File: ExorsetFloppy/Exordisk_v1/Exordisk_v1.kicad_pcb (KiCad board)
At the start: 2 copper layers, 160 x 100 mm, 105 parts, among them J1 BUS, J10 Conn_01x01, J11 Conn_01x01, J12 Conn_01x01, J13 Conn_01x01, J14 Conn_01x01, J15 Conn_01x01, J16 Conn_01x01, J17 Conn_01x01, J18 Conn_01x01, J19 Conn_02x02_Odd_Even, J2 Floppy, J20 Conn_01x01, J21 Conn_01x01, J22 Conn_01x01, J23 Conn_01x01, J24 Conn_01x01, J25 Conn_01x01, J26 Conn_01x01, J27 Conn_01x01, J28 Conn_01x01, J29 Conn_01x01, J3 Conn_01x01, J30 Conn_01x01, J31 Conn_01x01, J32 Conn_01x01, J33 Conn_01x01, J34 Conn_01x01, J35 Conn_01x01, J36 Conn_01x01, J37 Conn_01x01, J38 Conn_01x01, J39 Conn_01x01, J4 Conn_01x01, J40 Conn_01x01, J41 Conn_01x01, J5 Conn_01x01, J6 Conn_01x01, J7 Conn_01x17, J8 Conn_01x01, J9 Conn_01x01, Q1 BC337, U1 GAL22V10, U10 GAL16V8, U11 74HCT74, U12 74HCT74, U15 74HCT04, U16 74HCT74, U17 74HCT00, U18 74HCT74, U19 74LS73, U2 74HCT74, U20 68B21, U21 MC4024, U22 74LS157, U23 74LS123, U24 74HCT164, U25 74LS04, U27 MC4044, U28 74F163, U29 74F163, U3 74HC245, U34 6852_DIL24, U4 MC8506_new, U5 74F163, U6 27C32, U7 74HCT240, U8 74HCT244, Y1 1M

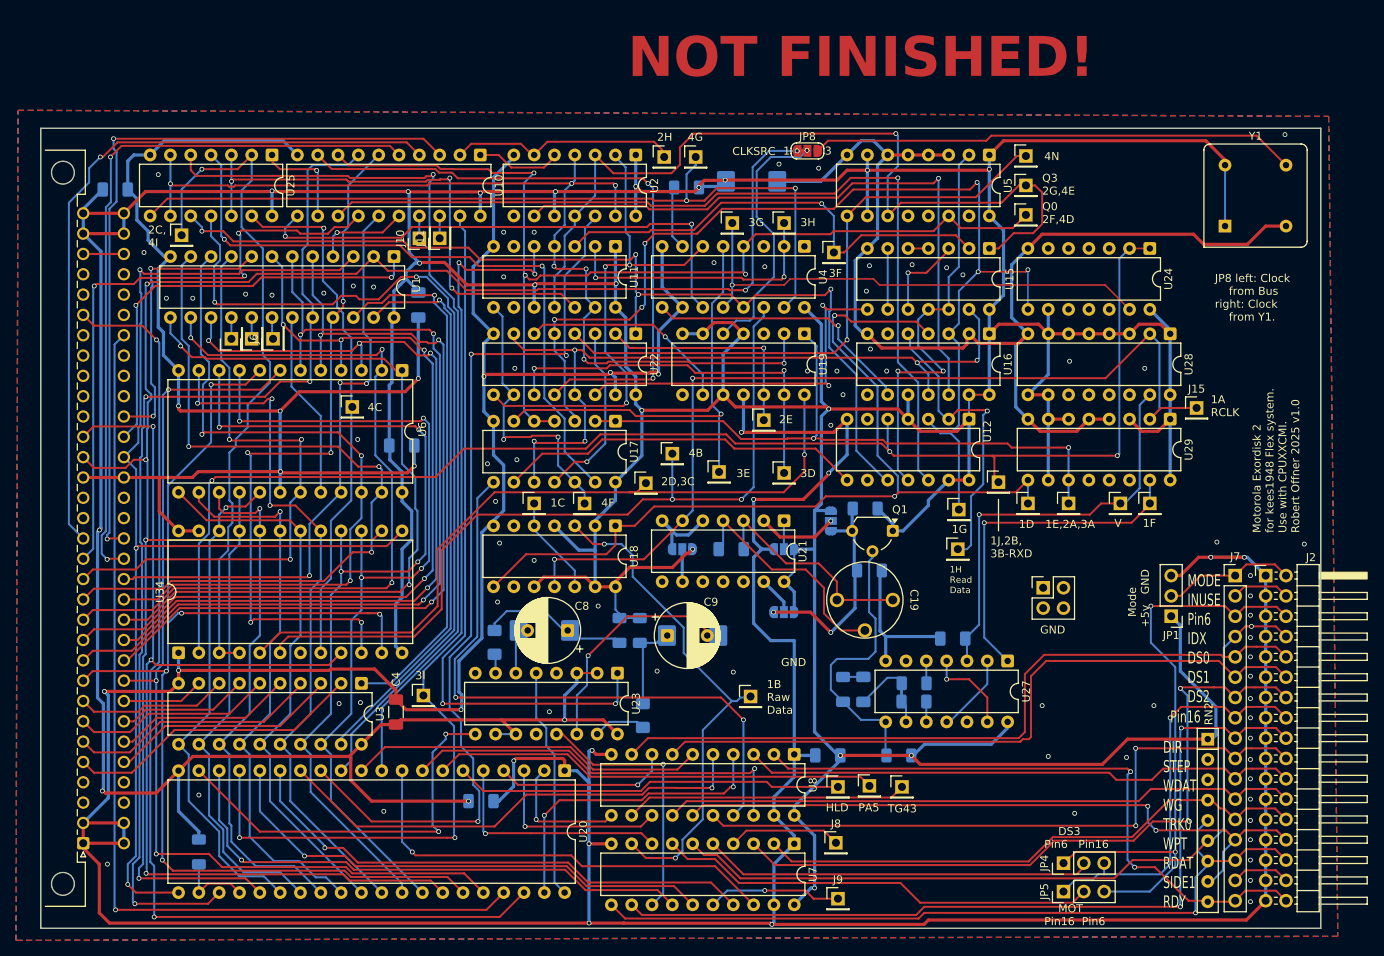
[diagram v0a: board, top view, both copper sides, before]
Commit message: new GAL eq. for additional EPROM on board
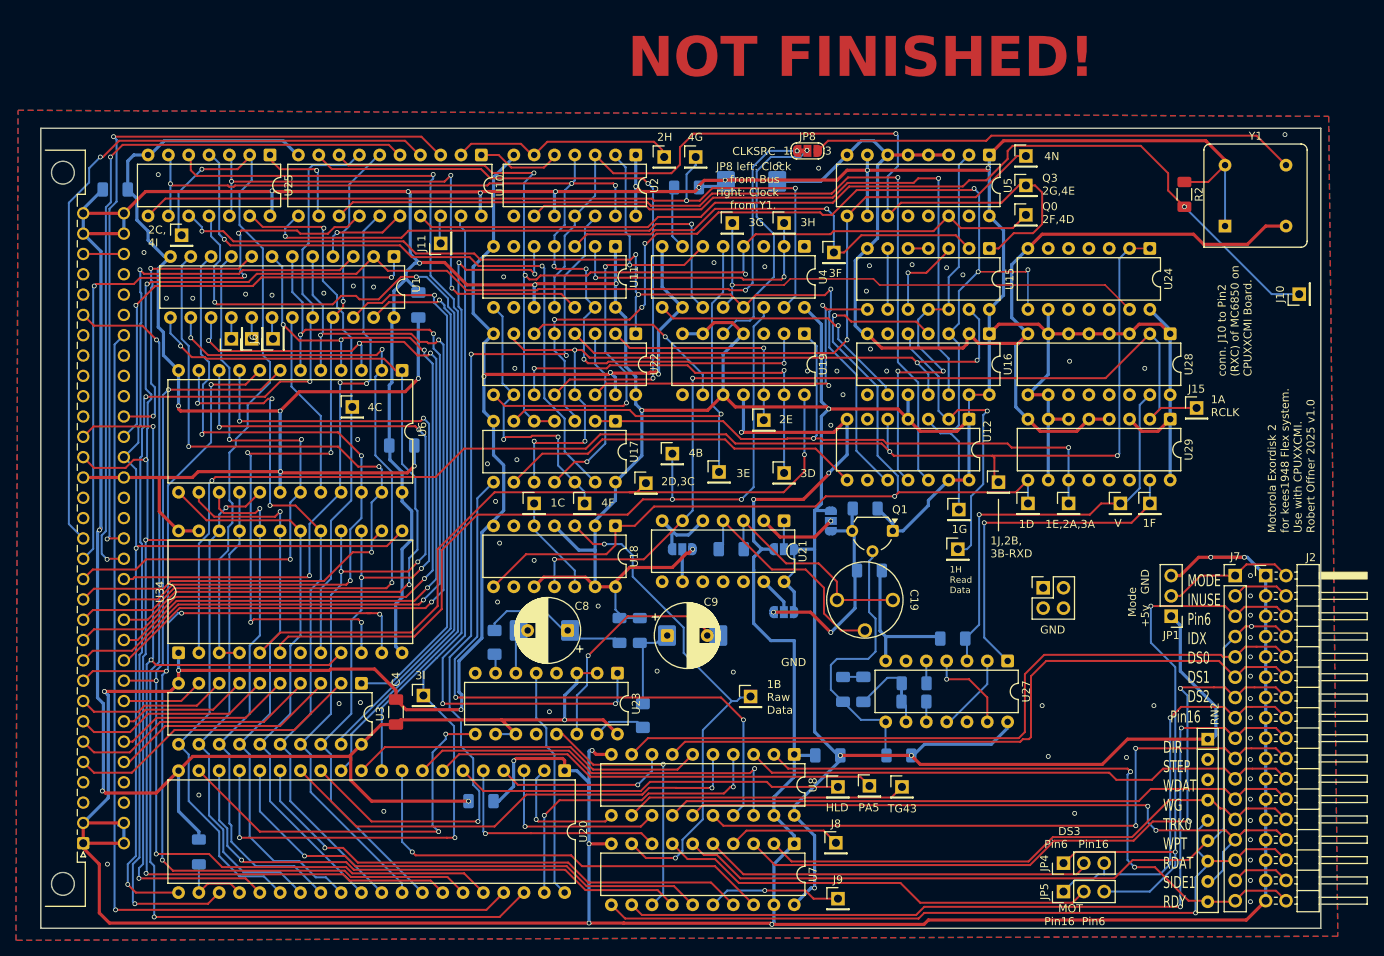
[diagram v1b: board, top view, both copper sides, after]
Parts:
- added R2: 10k, Resistor_SMD:R_1206_3216Metric_Pad1.30x1.75mm_HandSolder, F.Cu at (202.9, 58.3)
- moved J10 110.2 mm to (217.3, 70.7)
- moved J11 0.65 mm to (110.0, 64.4)
- moved U25 0.25 mm to (88.6, 53.3)
- moved U10 0.13 mm to (115.1, 53.3)
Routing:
- net Net-(J10-Pin_1): track 2.79 -> 124.2 mm, vias 0 -> 1
- net +5V: track 940.9 -> 947.2 mm
- net /Floppy Logic/~{8x_RD_CLK}: track 137.1 -> 136.0 mm
- net Net-(J11-Pin_1): track 2.79 -> 3.53 mm
- net Net-(J32-Pin_1): track 58.4 -> 57.7 mm
- net /Floppy Logic/~{TUF}: track 65.8 -> 66.4 mm
- net Net-(J20-Pin_1): track 86.0 -> 86.5 mm
- net /Floppy Logic/TUF: track 66.0 -> 66.6 mm
- net GND: track 918.0 -> 918.1 mm, vias 92 -> 88
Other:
- board text added: "conn. J10 to Pin2 (RXC) of MC6850 on CPUXXCMI Board."

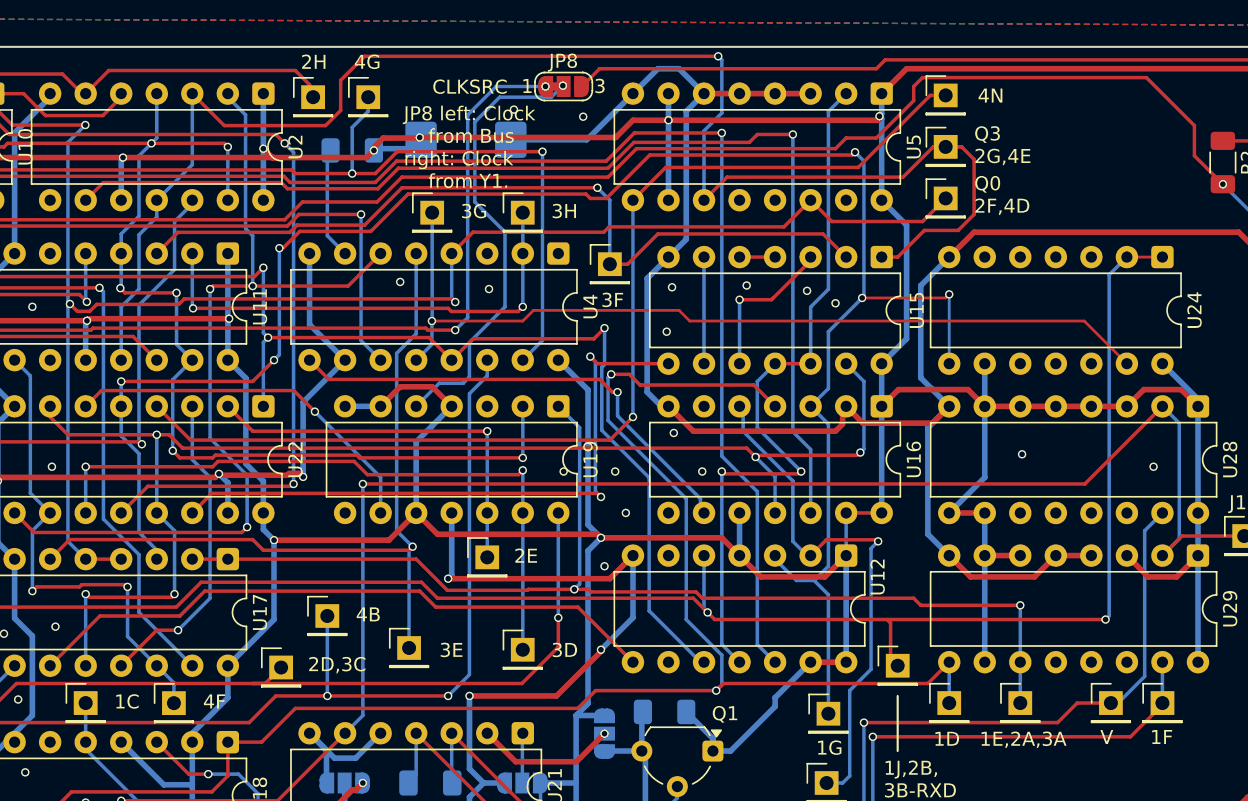
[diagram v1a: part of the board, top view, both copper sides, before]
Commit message: 74LS73 ch. to LS112
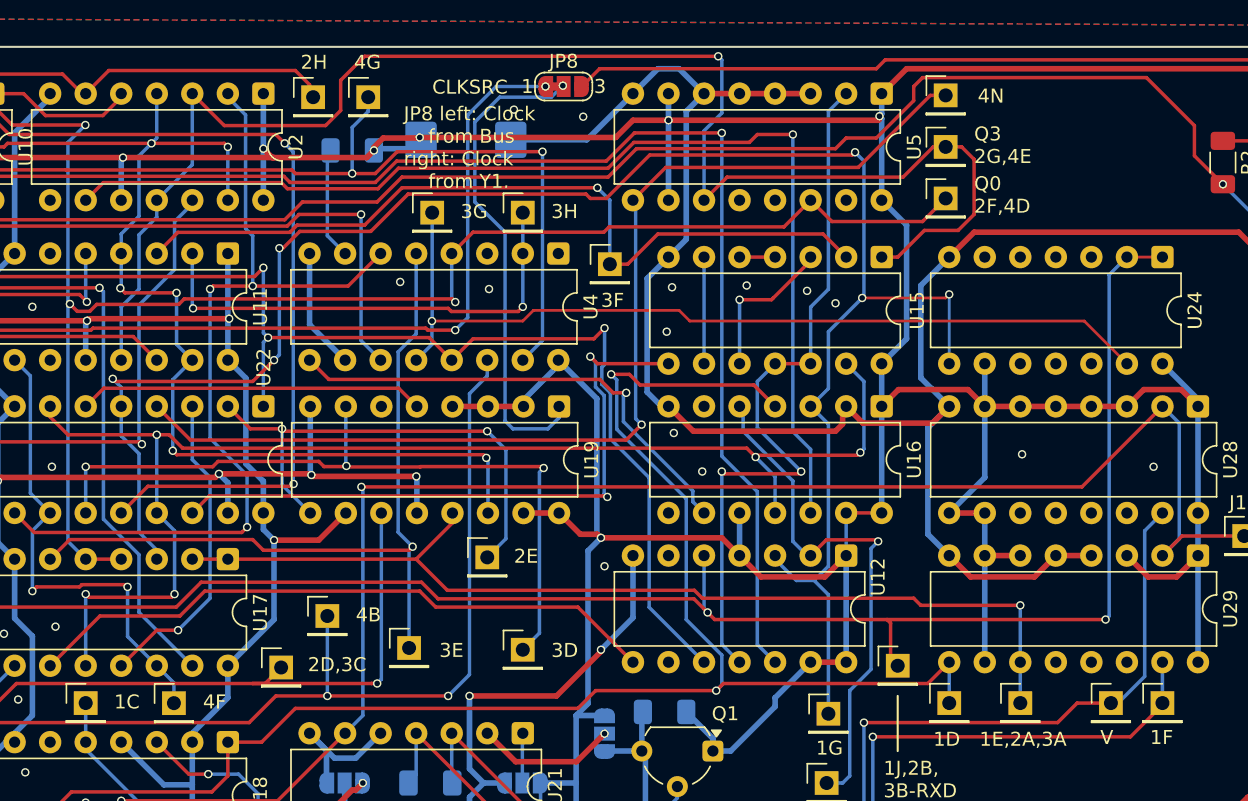
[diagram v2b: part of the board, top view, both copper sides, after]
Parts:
- U19: value 74LS73 -> 74LS112; footprint Package_DIP:DIP-14_W7.62mm -> Package_DIP:DIP-16_W7.62mm
- moved U19 0.05 mm to (155.5, 75.7)
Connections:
- U19 pad 1: /Floppy Logic/8x_RD_CLK -> Net-(JP8-C)
- U19 pad 11: GND -> Net-(J26-Pin_1)
- U19 pad 12: /Floppy Logic/SM_Latch -> GND
- U19 pad 13: /Floppy Logic/~{SM_Latch} -> /Floppy Logic/8x_RD_CLK
- U19 pad 14: Net-(J26-Pin_1) -> /Floppy Logic/RESET
- U19 pad 2: /Floppy Logic/RESET -> +5V
- U19 pad 3: GND -> +5V
- U19 pad 5: Net-(JP8-C) -> /Floppy Logic/CLK500k
- U19 pad 6: +5V -> unconnected-(U19A-~{Q}-Pad6)
- U19 pad 7: +5V -> /Floppy Logic/~{SM_Latch}
- U19 pad 8: unconnected-(U19A-~{Q}-Pad8) -> GND
- U19 pad 9: /Floppy Logic/CLK500k -> /Floppy Logic/SM_Latch
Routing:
- net +5V: track 947.2 -> 926.5 mm
- net GND: track 918.1 -> 905.3 mm, vias 88 -> 85
- net Net-(J26-Pin_1): track 93.7 -> 82.4 mm
- net /Floppy Logic/8x_RD_CLK: track 81.5 -> 71.9 mm, vias 2 -> 1
- net /Floppy Logic/SM_Latch: track 28.3 -> 36.3 mm, vias 1 -> 2
- net /Floppy Logic/~{SM_Latch}: track 48.1 -> 54.3 mm, vias 2 -> 3
- net Net-(JP8-C): track 32.2 -> 34.9 mm
- net /Floppy Logic/RESET: track 128.3 -> 125.8 mm
- net /Floppy Logic/CLK500k: track 26.7 -> 24.7 mm, vias 1 -> 0
- net Net-(J41-Pin_1): track 76.7 -> 77.9 mm
- net /Floppy Logic/~{8x_RD_CLK}: track 136.0 -> 137.1 mm
- net Net-(U16B-Q): track 34.2 -> 34.7 mm

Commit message: build script new
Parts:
- removed U6: 27C32, Package_DIP:DIP-24_W15.24mm
- added J42: Conn_01x01, Connector_PinHeader_2.54mm:PinHeader_1x01_P2.54mm_Vertical, F.Cu at (173.9, 132.3)
- added J43: Conn_01x01, Connector_PinHeader_2.54mm:PinHeader_1x01_P2.54mm_Vertical, F.Cu at (177.8, 132.3)
- added JP9: SolderJumper_2_Open, Jumper:SolderJumper-2_P1.3mm_Open_Pad1.0x1.5mm, B.Cu at (109.5, 84.1)
- added U14: 27C64, Package_DIP:DIP-28_W15.24mm, F.Cu at (109.5, 80.3)
- added U9: 74LS138, Package_DIP:DIP-16_W7.62mm, F.Cu at (164.2, 146.3)
- moved U7 0.51 mm to (154.2, 138.9)
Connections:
- U7 pad 15: /Floppy Logic/DS3 -> unconnected-(U7-I2b-Pad15)
- U7 pad 17: /Floppy Logic/DS2 -> unconnected-(U7-I3b-Pad17)
- U7 pad 3: /Floppy Logic/~{DS2} -> unconnected-(U7-O3b-Pad3)
- U7 pad 5: /Floppy Logic/~{DS3} -> unconnected-(U7-O2b-Pad5)
- U8 pad 11: /Floppy Logic/DS0 -> unconnected-(U8-I0b-Pad11)
- U8 pad 13: /Floppy Logic/DS1 -> unconnected-(U8-I1b-Pad13)
- U8 pad 7: /Floppy Logic/~{DS1} -> unconnected-(U8-O1b-Pad7)
- U8 pad 9: /Floppy Logic/~{DS0} -> unconnected-(U8-O0b-Pad9)
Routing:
- net /Floppy Logic/DS3: track 64.0 -> 111.1 mm, vias 1 -> 2
- net /Floppy Logic/DS0: track 16.3 -> 56.2 mm
- net GND: track 905.3 -> 945.0 mm, vias 85 -> 114
- net /Floppy Logic/DS2: track 66.0 -> 102.6 mm, vias 1 -> 2
- net /Floppy Logic/DS1: track 23.5 -> 59.9 mm
- net /BA12: track 76.0 -> 108.1 mm, vias 3 -> 4
- net +5V: track 926.5 -> 956.8 mm, vias 22 -> 23
- net /Floppy Logic/~{DS3}: track 48.8 -> 20.4 mm, vias 0 -> 1
- net /Floppy Logic/~{DS0}: track 92.3 -> 64.5 mm, vias 0 -> 1
- net /BA4: track 107.4 -> 82.1 mm, vias 4 -> 5
- net /Floppy Logic/HLD: track 49.0 -> 71.1 mm
- net /D0: track 109.5 -> 88.3 mm, vias 4 -> 2
- net /Floppy Logic/~{DS1}: track 87.9 -> 67.3 mm, vias 0 -> 1
- net /Floppy Logic/~{DS2}: track 89.8 -> 73.5 mm, vias 2 -> 3
- net /D1: track 112.2 -> 96.8 mm, vias 4 -> 1
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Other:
- board text added: "PB5"
- board text added: "PB6"

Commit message: new build for extra drives
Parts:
- removed J42, J43: Conn_01x01, Connector_PinHeader_2.54mm:PinHeader_1x01_P2.54mm_Vertical
- added R5: 1k, Resistor_SMD:R_1206_3216Metric_Pad1.30x1.75mm_HandSolder, B.Cu at (167.4, 129.0)
- U9: value 74LS138 -> 74LS139
- moved R16 1.78 mm to (167.4, 126.6)
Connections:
- J8 pad 1: Net-(J8-Pin_1) -> unconnected-(J8-Pin_1-Pad1)
- J9 pad 1: Net-(J9-Pin_1) -> unconnected-(J9-Pin_1-Pad1)
- U7 pad 16: Net-(J9-Pin_1) -> /Floppy Logic/WPROT
- U7 pad 4: Net-(J8-Pin_1) -> /Floppy Logic/~{WPT}
- U8 pad 15: /Floppy Logic/~{WPT} -> /Floppy Logic/DS3
- U8 pad 5: /Floppy Logic/WPROT -> /Floppy Logic/~{SIDE1}
- U9 pad 1: /Floppy Logic/DS0 -> /Floppy Logic/HLD
- U9 pad 12: /Floppy Logic/~{DS3} -> /Floppy Logic/~{DS0}
- U9 pad 13: /Floppy Logic/~{DS0} -> GND
- U9 pad 14: /Floppy Logic/~{DS1} -> /Floppy Logic/DS0
- U9 pad 15: /Floppy Logic/~{DS2} -> /Floppy Logic/HLD
- U9 pad 2: /Floppy Logic/DS1 -> /Floppy Logic/DS2
- U9 pad 3: GND -> /Floppy Logic/DS1
- U9 pad 4: GND -> /Floppy Logic/~{DS3}
- U9 pad 5: /Floppy Logic/HLD -> /Floppy Logic/~{DS1}
- U9 pad 6: +5V -> /Floppy Logic/~{DS2}
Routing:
- net /Floppy Logic/~{SIDE1}: track 7.40 -> 92.7 mm, vias 0 -> 1
- net /Floppy Logic/DS3: track 111.1 -> 65.1 mm, vias 2 -> 3
- net Net-(J9-Pin_1): track 16.7 -> 0.00 mm, vias 1 -> 0
- net /Floppy Logic/DS2: track 102.6 -> 86.0 mm, vias 2 -> 1
- net +5V: track 956.8 -> 940.6 mm, vias 23 -> 22
- net Net-(J8-Pin_1): track 13.9 -> 0.00 mm
- net GND: track 945.0 -> 955.4 mm, vias 114 -> 122
- net /Floppy Logic/~{DS2}: track 73.5 -> 64.8 mm
- net /Floppy Logic/~{WPT}: track 85.6 -> 78.8 mm
- net /Floppy Logic/DS0: track 56.2 -> 62.3 mm, vias 1 -> 2
- net /Floppy Logic/RAW_DATA: track 64.8 -> 59.0 mm, vias 2 -> 1
- net /Floppy Logic/~{DS1}: track 67.3 -> 61.9 mm
- net /Floppy Logic/PA5: track 55.8 -> 60.5 mm
- net /Floppy Logic/~{DS3}: track 20.4 -> 23.8 mm
- net /Floppy Logic/HLD: track 71.1 -> 68.2 mm
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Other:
- board text removed: "PB5"
- board text removed: "PB6"

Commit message: Exordisk Board continued
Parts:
- added D3: 1N4148, Diode_SMD:D_1206_3216Metric_Pad1.42x1.75mm_HandSolder, B.Cu at (180.7, 131.7)
- added D4: 1N4148, Diode_SMD:D_1206_3216Metric_Pad1.42x1.75mm_HandSolder, B.Cu at (186.0, 131.7)
- added D5: 1N4148, Diode_SMD:D_1206_3216Metric_Pad1.42x1.75mm_HandSolder, F.Cu at (189.4, 124.0)
- added D6: 1N4148, Diode_SMD:D_1206_3216Metric_Pad1.42x1.75mm_HandSolder, F.Cu at (184.3, 124.0)
- added J42: SS/DS, Connector_PinHeader_2.54mm:PinHeader_2x04_P2.54mm_Vertical, F.Cu at (192.8, 112.8)
- added R10: 1k, Resistor_SMD:R_1206_3216Metric_Pad1.30x1.75mm_HandSolder, F.Cu at (184.0, 105.3)
- added R6: 1k, Resistor_SMD:R_1206_3216Metric_Pad1.30x1.75mm_HandSolder, F.Cu at (184.0, 107.7)
- added R8: 1k, Resistor_SMD:R_1206_3216Metric_Pad1.30x1.75mm_HandSolder, F.Cu at (184.0, 110.4)
- added R9: 1k, Resistor_SMD:R_1206_3216Metric_Pad1.30x1.75mm_HandSolder, F.Cu at (184.0, 112.9)
- added U6: 74LS139, Package_DIP:DIP-16_W7.62mm, F.Cu at (164.2, 146.3)
- U9: value 74LS139 -> 74LS32; footprint Package_DIP:DIP-16_W7.62mm -> Package_DIP:DIP-14_W7.62mm
- moved J19 28.5 mm to (207.5, 89.5)
- moved U9 14.7 mm to (174.1, 135.5)
- moved JP1 11.8 mm to (207.5, 101.0)
- moved R5 0.05 mm to (167.4, 129.0)
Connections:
- U9 pad 1: /Floppy Logic/HLD -> /Floppy Logic/L0
- U9 pad 10: unconnected-(U9B-O2-Pad10) -> /Floppy Logic/~{DS2}
- U9 pad 11: unconnected-(U9B-O1-Pad11) -> Net-(D6-A)
- U9 pad 12: /Floppy Logic/~{DS0} -> /Floppy Logic/L3
- U9 pad 13: GND -> /Floppy Logic/~{DS3}
- U9 pad 14: /Floppy Logic/DS0 -> +5V
- U9 pad 2: /Floppy Logic/DS2 -> /Floppy Logic/~{DS0}
- U9 pad 3: /Floppy Logic/DS1 -> Net-(D3-A)
- U9 pad 4: /Floppy Logic/~{DS3} -> /Floppy Logic/L1
- U9 pad 6: /Floppy Logic/~{DS2} -> Net-(D4-A)
- U9 pad 7: unconnected-(U9A-O3-Pad7) -> GND
- U9 pad 8: GND -> Net-(D5-A)
- U9 pad 9: unconnected-(U9B-O3-Pad9) -> /Floppy Logic/L2
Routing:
- net /Floppy Logic/L1: track 0.00 -> 40.1 mm, vias 0 -> 2
- net /Floppy Logic/PA5: track 60.5 -> 96.5 mm, vias 0 -> 3
- net /Floppy Logic/L0: track 0.00 -> 33.3 mm, vias 0 -> 1
- net /Floppy Logic/L3: track 0.00 -> 30.0 mm
- net /Floppy Logic/DS1: track 61.6 -> 32.4 mm
- net /Floppy Logic/L2: track 0.00 -> 26.6 mm, vias 0 -> 1
- net /Floppy Logic/~{DS3}: track 23.8 -> 41.8 mm
- net /Floppy Logic/~{DS2}: track 64.8 -> 81.1 mm, vias 3 -> 4
- net GND: track 955.4 -> 970.7 mm, vias 122 -> 116
- net +5V: track 940.6 -> 954.0 mm
- net /Floppy Logic/~{DS0}: track 65.5 -> 73.9 mm, vias 1 -> 2
- net /Floppy Logic/F_B: track 76.9 -> 69.8 mm
- net /Floppy Logic/~{WPT}: track 78.8 -> 83.2 mm
- net Net-(D4-A): track 0.00 -> 4.07 mm
- net /Floppy Logic/DS0: track 62.3 -> 58.3 mm, vias 2 -> 1
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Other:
- board text added: "DS3 DS2 DS1 DS0"
- board text added: "SS/DS"
